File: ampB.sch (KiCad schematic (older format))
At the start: 13 parts, among them U2 screw_term, U4 screw_term, U7 TL084, U8 screw_term

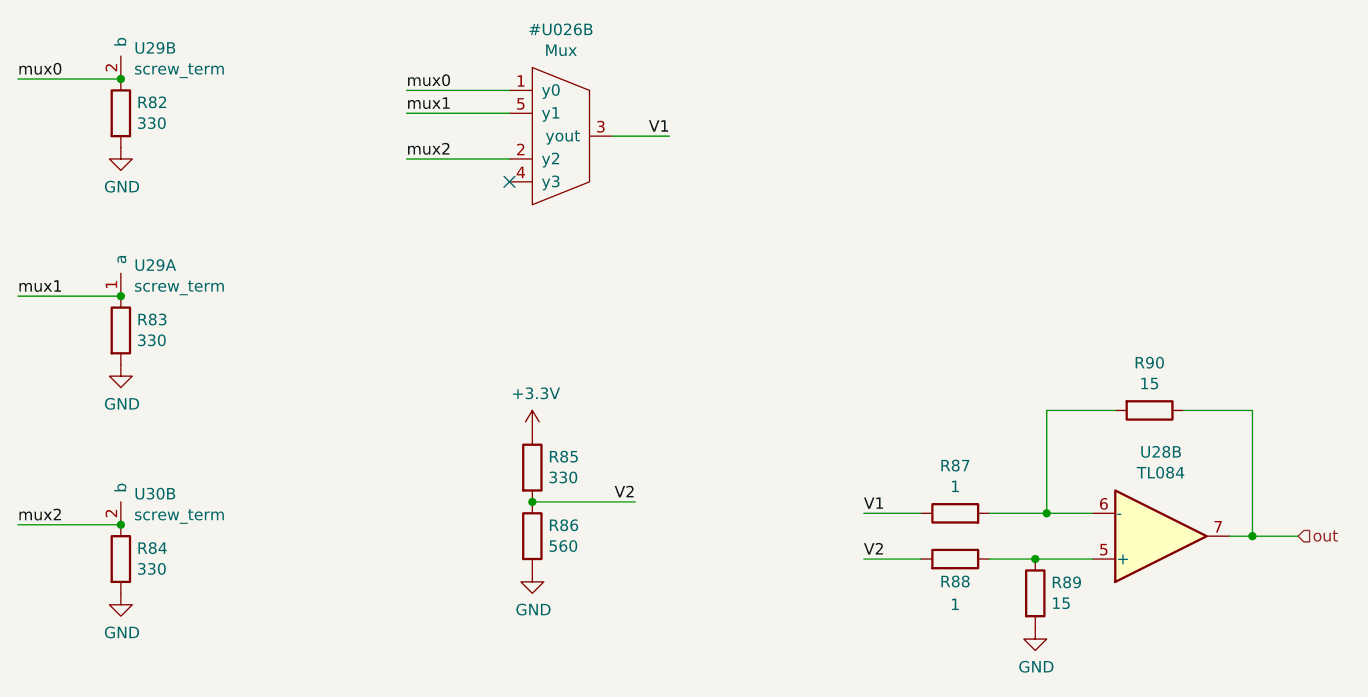
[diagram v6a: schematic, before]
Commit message: added all muxes to the board
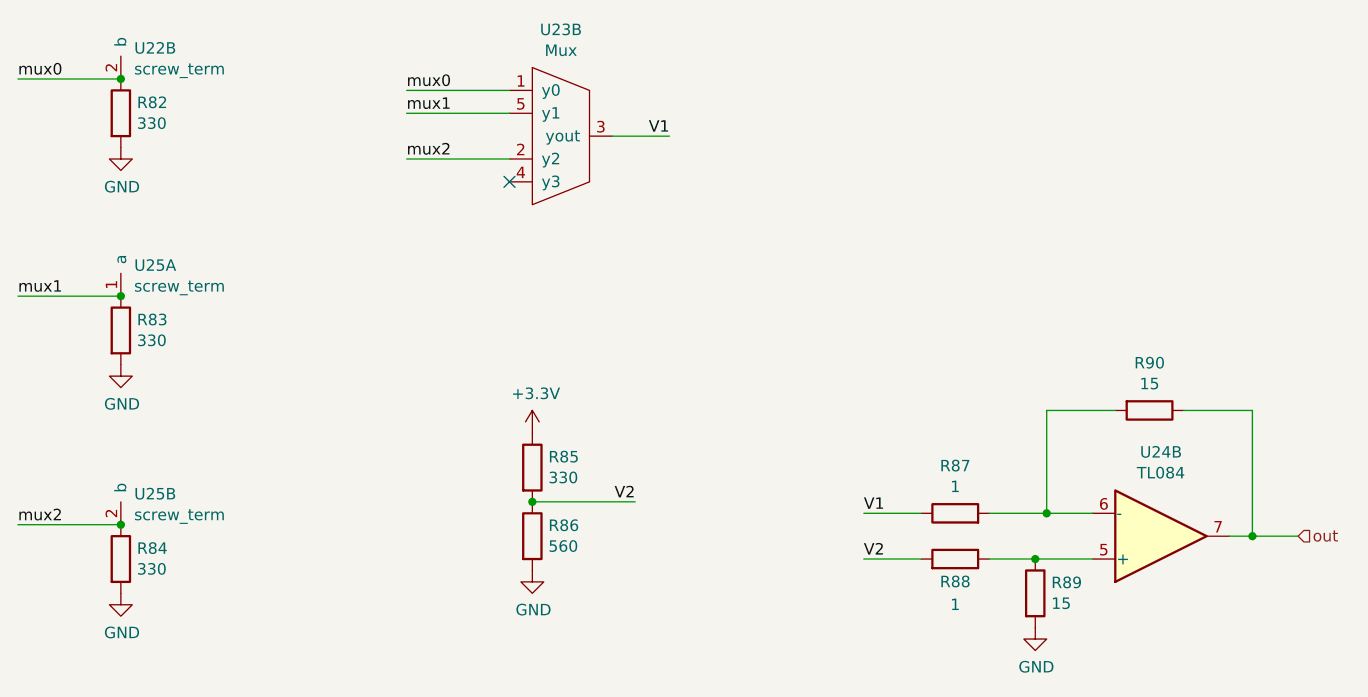
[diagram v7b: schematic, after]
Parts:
- added U5: Mux, Package_DIP:DIP-16_W7.62mm, symbol PNG_PCB_Parts:Mux
- renumbered U2 to U4, U7 to U6, U8 to U7, U4 to U7
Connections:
- net V1: now also U5.3 (yout)
- net mux0: now also U5.1 (y0)
- net mux1: now also U5.5 (y1)
- net mux2: now also U5.2 (y2)
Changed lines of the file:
@@
 AR Path="/6017CC5E/6019E3A6" Ref="U?"  Part="1"
 AR Path="/6017DA21/6019E3A6" Ref="U?"  Part="1"
-AR Path="/601927EB/6019E3A6" Ref="U7"  Part="2"
+AR Path="/601927EB/6019E3A6" Ref="U6"  Part="2"
 AR Path="/6019DBCE/6019E3A6" Ref="U?"  Part="2"
-AR Path="/601B4C11/6019E3A6" Ref="U12"  Part="2"
-AR Path="/601B73BA/6019E3A6" Ref="U28"  Part="2"
-F 0 "U28" H 6000 3433 50  0000 C CNN
+AR Path="/601B4C11/6019E3A6" Ref="U15"  Part="2"
+AR Path="/601B73BA/6019E3A6" Ref="U24"  Part="2"
+F 0 "U24" H 6000 3433 50  0000 C CNN
 F 1 "TL084" H 6000 3524 50  0000 C CNN
 F 2 "Package_DIP:DIP-14_W7.62mm" H 5950 3900 50  0001 C CNN
@@
 	1    0    0    -1
 $EndComp
-$Comp
-L PNG_PCB_Parts:Mux U?
-U 2 1 60198F2C
-P 3350 2050
-AR Path="/60132BC3/6013AE22/60198F2C" Ref="U?"  Part="1"
-AR Path="/6017CC5E/60198F2C" Ref="U?"  Part="1"
-AR Path="/6017DA21/60198F2C" Ref="U?"  Part="1"
-AR Path="/601927EB/60198F2C" Ref="#U05"  Part="2"
-AR Path="/6019DBCE/60198F2C" Ref="U?"  Part="2"
-AR Path="/601B4C11/60198F2C" Ref="#U016"  Part="2"
-AR Path="/601B73BA/60198F2C" Ref="#U026"  Part="2"
-F 0 "#U026" H 3375 2515 50  0000 C CNN
-F 1 "Mux" H 3375 2424 50  0000 C CNN
-F 2 "Package_DIP:DIP-16_W7.62mm" H 3350 2050 50  0001 C CNN
-F 3 "http://www.ti.com/lit/ds/symlink/tl081.pdf" H 3350 2050 50  0001 C CNN
-	2    3350 2050
-	1    0    0    -1
-$EndComp
 Wire Wire Line
 	1450 1800 1000 1800
@@
 AR Path="/6017CC5E/60198F2E" Ref="U?"  Part="2"
 AR Path="/6017DA21/60198F2E" Ref="U?"  Part="1"
-AR Path="/601927EB/60198F2E" Ref="U8"  Part="1"
+AR Path="/601927EB/60198F2E" Ref="U7"  Part="1"
 AR Path="/6019DBCE/60198F2E" Ref="U?"  Part="1"
-AR Path="/601B4C11/60198F2E" Ref="U18"  Part="1"
-AR Path="/601B73BA/60198F2E" Ref="U29"  Part="1"
-F 0 "U29" H 1508 2884 50  0000 L CNN
+AR Path="/601B4C11/60198F2E" Ref="U16"  Part="1"
+AR Path="/601B73BA/60198F2E" Ref="U25"  Part="1"
+F 0 "U25" H 1508 2884 50  0000 L CNN
 F 1 "screw_term" H 1508 2793 50  0000 L CNN
 F 2 "Connector_PinHeader_1.27mm:PinHeader_1x02_P1.27mm_Vertical" H 1450 2750 50  0001 C CNN
@@
 AR Path="/6017CC5E/6019A2A3" Ref="U?"  Part="2"
 AR Path="/6017DA21/6019A2A3" Ref="U?"  Part="1"
-AR Path="/601927EB/6019A2A3" Ref="U2"  Part="2"
+AR Path="/601927EB/6019A2A3" Ref="U4"  Part="2"
 AR Path="/6019DBCE/6019A2A3" Ref="U?"  Part="2"
-AR Path="/601B4C11/6019A2A3" Ref="U18"  Part="2"
-AR Path="/601B73BA/6019A2A3" Ref="U29"  Part="2"
-F 0 "U29" H 1508 1934 50  0000 L CNN
+AR Path="/601B4C11/6019A2A3" Ref="U13"  Part="2"
+AR Path="/601B73BA/6019A2A3" Ref="U22"  Part="2"
+F 0 "U22" H 1508 1934 50  0000 L CNN
 F 1 "screw_term" H 1508 1843 50  0000 L CNN
 F 2 "Connector_PinHeader_1.27mm:PinHeader_1x02_P1.27mm_Vertical" H 1450 1800 50  0001 C CNN
@@
 AR Path="/6017CC5E/6019E3B8" Ref="U?"  Part="2"
 AR Path="/6017DA21/6019E3B8" Ref="U?"  Part="1"
-AR Path="/601927EB/6019E3B8" Ref="U4"  Part="2"
+AR Path="/601927EB/6019E3B8" Ref="U7"  Part="2"
 AR Path="/6019DBCE/6019E3B8" Ref="U?"  Part="2"
-AR Path="/601B4C11/6019E3B8" Ref="U19"  Part="2"
-AR Path="/601B73BA/6019E3B8" Ref="U30"  Part="2"
-F 0 "U30" H 1508 3884 50  0000 L CNN
+AR Path="/601B4C11/6019E3B8" Ref="U16"  Part="2"
+AR Path="/601B73BA/6019E3B8" Ref="U25"  Part="2"
+F 0 "U25" H 1508 3884 50  0000 L CNN
 F 1 "screw_term" H 1508 3793 50  0000 L CNN
 F 2 "Connector_PinHeader_1.27mm:PinHeader_1x02_P1.27mm_Vertical" H 1450 3750 50  0001 C CNN
@@
 $EndComp
 Connection ~ 1450 3750
+$Comp
+L PNG_PCB_Parts:Mux U5
+U 2 1 6017859B
+P 3350 2050
+AR Path="/601927EB/6017859B" Ref="U5"  Part="2"
+AR Path="/601B4C11/6017859B" Ref="U14"  Part="2"
+AR Path="/601B73BA/6017859B" Ref="U23"  Part="2"
+F 0 "U23" H 3375 2515 50  0000 C CNN
+F 1 "Mux" H 3375 2424 50  0000 C CNN
+F 2 "Package_DIP:DIP-16_W7.62mm" H 3350 2050 50  0001 C CNN
+F 3 "" H 3350 2050 50  0001 C CNN
+	2    3350 2050
+	1    0    0    -1
+$EndComp
 $EndSCHEMATC

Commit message: changed to mcp6004 op amp
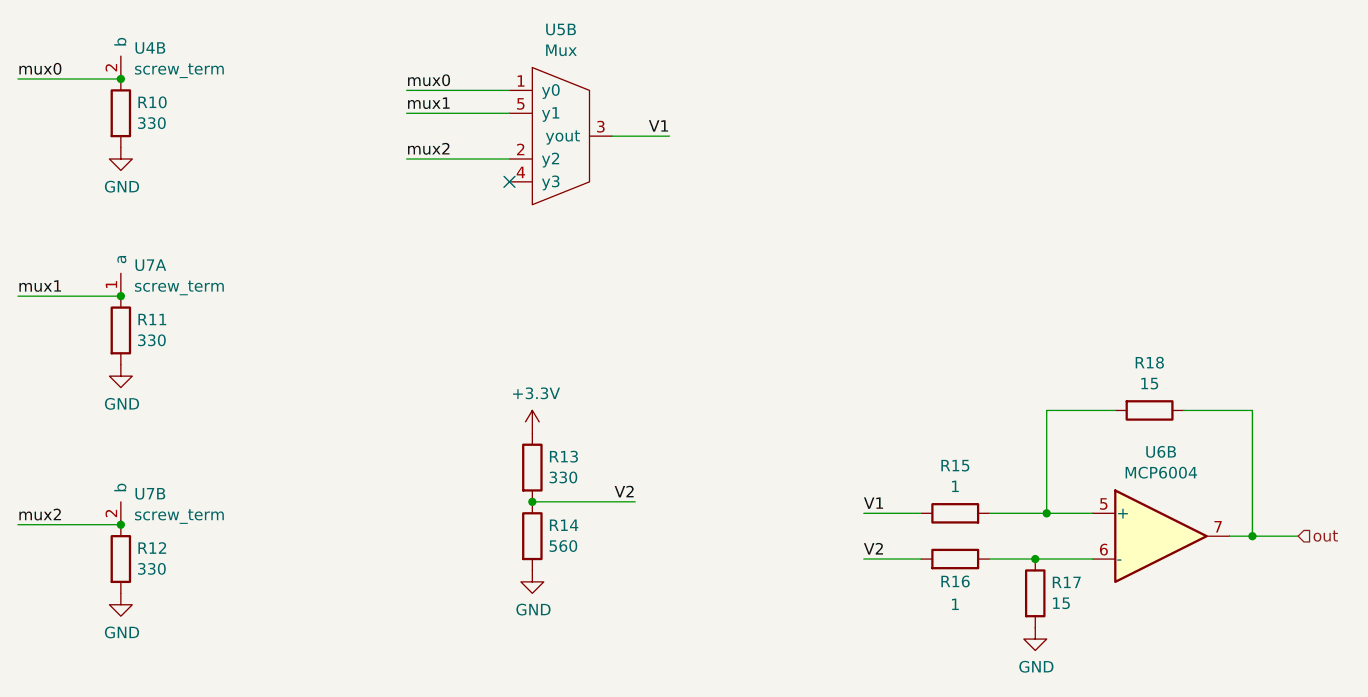
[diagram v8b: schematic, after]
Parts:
- removed U6: TL084, Package_DIP:DIP-14_W7.62mm, symbol Amplifier_Operational:TL084
- added U6: MCP6004, Package_DIP:DIP-14_W7.62mm, symbol Amplifier_Operational:MCP6004
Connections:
- net out: now also U6.7
- net at R15.2, R18.2: now also U6.5 (+)
- net at R16.1, R17.1: now also U6.6 (-)
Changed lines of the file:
@@
 $Descr A4 11693 8268
 encoding utf-8
-Sheet 11 11
+Sheet 3 11
 Title ""
 Date ""
@@
 AR Path="/601B4C11/6019E3AB" Ref="#PWR048"  Part="1"
 AR Path="/601B73BA/6019E3AB" Ref="#PWR078"  Part="1"
-F 0 "#PWR078" H 1450 1850 50  0001 C CNN
+F 0 "#PWR018" H 1450 1850 50  0001 C CNN
 F 1 "GND" H 1455 1927 50  0000 C CNN
 F 2 "" H 1450 2100 50  0001 C CNN
@@
 	1    1450 2100
 	1    0    0    -1
-$EndComp
-$Comp
-L Amplifier_Operational:TL084 U?
-U 2 1 6019E3A6
-P 6000 3800
-AR Path="/60132BC3/6013AE22/6019E3A6" Ref="U?"  Part="1"
-AR Path="/6017CC5E/6019E3A6" Ref="U?"  Part="1"
-AR Path="/6017DA21/6019E3A6" Ref="U?"  Part="1"
-AR Path="/601927EB/6019E3A6" Ref="U6"  Part="2"
-AR Path="/6019DBCE/6019E3A6" Ref="U?"  Part="2"
-AR Path="/601B4C11/6019E3A6" Ref="U15"  Part="2"
-AR Path="/601B73BA/6019E3A6" Ref="U24"  Part="2"
-F 0 "U24" H 6000 3433 50  0000 C CNN
-F 1 "TL084" H 6000 3524 50  0000 C CNN
-F 2 "Package_DIP:DIP-14_W7.62mm" H 5950 3900 50  0001 C CNN
-F 3 "http://www.ti.com/lit/ds/symlink/tl081.pdf" H 6050 4000 50  0001 C CNN
-	2    6000 3800
-	1    0    0    1
 $EndComp
 $Comp
@@
 AR Path="/601B4C11/6019E3A5" Ref="R53"  Part="1"
 AR Path="/601B73BA/6019E3A5" Ref="R89"  Part="1"
-F 0 "R89" H 5520 4096 50  0000 L CNN
+F 0 "R17" H 5520 4096 50  0000 L CNN
 F 1 "15" H 5520 4005 50  0000 L CNN
 F 2 "Resistor_THT:R_Axial_DIN0204_L3.6mm_D1.6mm_P5.08mm_Horizontal" V 5380 4050 50  0001 C CNN
@@
 AR Path="/601B4C11/6017E430" Ref="R54"  Part="1"
 AR Path="/601B73BA/6017E430" Ref="R90"  Part="1"
-F 0 "R90" V 5743 3250 50  0000 C CNN
+F 0 "R18" V 5743 3250 50  0000 C CNN
 F 1 "15" V 5834 3250 50  0000 C CNN
 F 2 "Resistor_THT:R_Axial_DIN0204_L3.6mm_D1.6mm_P5.08mm_Horizontal" V 5880 3250 50  0001 C CNN
@@
 AR Path="/601B4C11/60198F33" Ref="R51"  Part="1"
 AR Path="/601B73BA/60198F33" Ref="R87"  Part="1"
-F 0 "R87" V 5307 3700 50  0000 C CNN
+F 0 "R15" V 5307 3700 50  0000 C CNN
 F 1 "1" V 5216 3700 50  0000 C CNN
 F 2 "Resistor_THT:R_Axial_DIN0204_L3.6mm_D1.6mm_P5.08mm_Horizontal" V 5030 3700 50  0001 C CNN
@@
 AR Path="/601B4C11/6017E432" Ref="R52"  Part="1"
 AR Path="/601B73BA/6017E432" Ref="R88"  Part="1"
-F 0 "R88" V 5000 3900 50  0000 C CNN
+F 0 "R16" V 5000 3900 50  0000 C CNN
 F 1 "1" V 4900 3900 50  0000 C CNN
 F 2 "Resistor_THT:R_Axial_DIN0204_L3.6mm_D1.6mm_P5.08mm_Horizontal" V 5030 3900 50  0001 C CNN
@@
 AR Path="/601B4C11/60198F35" Ref="R49"  Part="1"
 AR Path="/601B73BA/60198F35" Ref="R85"  Part="1"
-F 0 "R85" H 3320 3546 50  0000 L CNN
+F 0 "R13" H 3320 3546 50  0000 L CNN
 F 1 "330" H 3320 3455 50  0000 L CNN
 F 2 "Resistor_THT:R_Axial_DIN0204_L3.6mm_D1.6mm_P5.08mm_Horizontal" V 3180 3500 50  0001 C CNN
@@
 AR Path="/601B4C11/6019E3B4" Ref="R50"  Part="1"
 AR Path="/601B73BA/6019E3B4" Ref="R86"  Part="1"
-F 0 "R86" H 3320 3846 50  0000 L CNN
+F 0 "R14" H 3320 3846 50  0000 L CNN
 F 1 "560" H 3320 3755 50  0000 L CNN
 F 2 "Resistor_THT:R_Axial_DIN0204_L3.6mm_D1.6mm_P5.08mm_Horizontal" V 3180 3800 50  0001 C CNN
@@
 AR Path="/601B4C11/6019E3B5" Ref="#PWR051"  Part="1"
 AR Path="/601B73BA/6019E3B5" Ref="#PWR081"  Part="1"
-F 0 "#PWR081" H 3250 3200 50  0001 C CNN
+F 0 "#PWR021" H 3250 3200 50  0001 C CNN
 F 1 "+3.3V" H 3265 3523 50  0000 C CNN
 F 2 "" H 3250 3350 50  0001 C CNN
@@
 AR Path="/601B4C11/6017E436" Ref="#PWR052"  Part="1"
 AR Path="/601B73BA/6017E436" Ref="#PWR082"  Part="1"
-F 0 "#PWR082" H 3250 3700 50  0001 C CNN
+F 0 "#PWR022" H 3250 3700 50  0001 C CNN
 F 1 "GND" H 3255 3777 50  0000 C CNN
 F 2 "" H 3250 3950 50  0001 C CNN
@@
 AR Path="/601B4C11/6019E3AC" Ref="#PWR053"  Part="1"
 AR Path="/601B73BA/6019E3AC" Ref="#PWR083"  Part="1"
-F 0 "#PWR083" H 5450 3950 50  0001 C CNN
+F 0 "#PWR023" H 5450 3950 50  0001 C CNN
 F 1 "GND" H 5455 4027 50  0000 C CNN
 F 2 "" H 5450 4200 50  0001 C CNN
@@
 AR Path="/601B4C11/60198F2A" Ref="R46"  Part="1"
 AR Path="/601B73BA/60198F2A" Ref="R82"  Part="1"
-F 0 "R82" H 1520 1996 50  0000 L CNN
+F 0 "R10" H 1520 1996 50  0000 L CNN
 F 1 "330" H 1520 1905 50  0000 L CNN
 F 2 "Resistor_THT:R_Axial_DIN0204_L3.6mm_D1.6mm_P5.08mm_Horizontal" V 1380 1950 50  0001 C CNN
@@
 AR Path="/601B4C11/60198F2D" Ref="#PWR049"  Part="1"
 AR Path="/601B73BA/60198F2D" Ref="#PWR079"  Part="1"
-F 0 "#PWR079" H 1450 2800 50  0001 C CNN
+F 0 "#PWR019" H 1450 2800 50  0001 C CNN
 F 1 "GND" H 1455 2877 50  0000 C CNN
 F 2 "" H 1450 3050 50  0001 C CNN
@@
 AR Path="/601B4C11/6017E43C" Ref="R47"  Part="1"
 AR Path="/601B73BA/6017E43C" Ref="R83"  Part="1"
-F 0 "R83" H 1520 2946 50  0000 L CNN
+F 0 "R11" H 1520 2946 50  0000 L CNN
 F 1 "330" H 1520 2855 50  0000 L CNN
 F 2 "Resistor_THT:R_Axial_DIN0204_L3.6mm_D1.6mm_P5.08mm_Horizontal" V 1380 2900 50  0001 C CNN
@@
 AR Path="/601B4C11/60198F2E" Ref="U16"  Part="1"
 AR Path="/601B73BA/60198F2E" Ref="U25"  Part="1"
-F 0 "U25" H 1508 2884 50  0000 L CNN
+F 0 "U7" H 1508 2884 50  0000 L CNN
 F 1 "screw_term" H 1508 2793 50  0000 L CNN
 F 2 "Connector_PinHeader_1.27mm:PinHeader_1x02_P1.27mm_Vertical" H 1450 2750 50  0001 C CNN
@@
 AR Path="/601B4C11/60198F2F" Ref="#PWR050"  Part="1"
 AR Path="/601B73BA/60198F2F" Ref="#PWR080"  Part="1"
-F 0 "#PWR080" H 1450 3800 50  0001 C CNN
+F 0 "#PWR020" H 1450 3800 50  0001 C CNN
 F 1 "GND" H 1455 3877 50  0000 C CNN
 F 2 "" H 1450 4050 50  0001 C CNN
@@
 AR Path="/601B4C11/6019E3B6" Ref="R48"  Part="1"
 AR Path="/601B73BA/6019E3B6" Ref="R84"  Part="1"
-F 0 "R84" H 1520 3946 50  0000 L CNN
+F 0 "R12" H 1520 3946 50  0000 L CNN
 F 1 "330" H 1520 3855 50  0000 L CNN
 F 2 "Resistor_THT:R_Axial_DIN0204_L3.6mm_D1.6mm_P5.08mm_Horizontal" V 1380 3900 50  0001 C CNN
@@
 AR Path="/601B4C11/6019A2A3" Ref="U13"  Part="2"
 AR Path="/601B73BA/6019A2A3" Ref="U22"  Part="2"
-F 0 "U22" H 1508 1934 50  0000 L CNN
+F 0 "U4" H 1508 1934 50  0000 L CNN
 F 1 "screw_term" H 1508 1843 50  0000 L CNN
 F 2 "Connector_PinHeader_1.27mm:PinHeader_1x02_P1.27mm_Vertical" H 1450 1800 50  0001 C CNN
@@
 AR Path="/601B4C11/6019E3B8" Ref="U16"  Part="2"
 AR Path="/601B73BA/6019E3B8" Ref="U25"  Part="2"
-F 0 "U25" H 1508 3884 50  0000 L CNN
+F 0 "U7" H 1508 3884 50  0000 L CNN
 F 1 "screw_term" H 1508 3793 50  0000 L CNN
 F 2 "Connector_PinHeader_1.27mm:PinHeader_1x02_P1.27mm_Vertical" H 1450 3750 50  0001 C CNN
@@
 AR Path="/601B4C11/6017859B" Ref="U14"  Part="2"
 AR Path="/601B73BA/6017859B" Ref="U23"  Part="2"
-F 0 "U23" H 3375 2515 50  0000 C CNN
+F 0 "U5" H 3375 2515 50  0000 C CNN
 F 1 "Mux" H 3375 2424 50  0000 C CNN
 F 2 "Package_DIP:DIP-16_W7.62mm" H 3350 2050 50  0001 C CNN
@@
 	1    0    0    -1
 $EndComp
+$Comp
+L Amplifier_Operational:MCP6004 U6
+U 2 1 6018C8DB
+P 6000 3800
+AR Path="/601927EB/6018C8DB" Ref="U6"  Part="2"
+AR Path="/601B4C11/6018C8DB" Ref="U15"  Part="2"
+AR Path="/601B73BA/6018C8DB" Ref="U24"  Part="2"
+F 0 "U6" H 6000 4167 50  0000 C CNN
+F 1 "MCP6004" H 6000 4076 50  0000 C CNN
+F 2 "Package_DIP:DIP-14_W7.62mm" H 5950 3900 50  0001 C CNN
+F 3 "http://ww1.microchip.com/downloads/en/DeviceDoc/21733j.pdf" H 6050 4000 50  0001 C CNN
+	2    6000 3800
+	1    0    0    -1
+$EndComp
